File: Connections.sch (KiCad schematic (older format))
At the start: 12 parts, among them P4 CONN_02X07, P6 CONN_02X07, P7 CONN_02X07, P8 CONN_02X07, SW1 SW_PUSH, SW2 SW_PUSH

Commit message: Layouting
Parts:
- added P2: CONN_02X03, w_pin_strip:pin_strip_3x2, symbol CONN_02X03
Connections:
- net C_IO2: now also P2.5 (P5); no longer P6.3 (P3)
- net C_IO3: now also P2.4 (P4); no longer P6.4 (P4)
- new net C_IO1: P2.3 (P3)
- new net C_IO4: P2.6 (P6)
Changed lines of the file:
@@
 	1    0    0    -1
 $EndComp
-Text Label 6450 3650 0    60   ~ 0
-C_IO3
-Text Label 5600 3650 0    60   ~ 0
-C_IO2
 $Comp
 L CONN_02X07 P6
@@
 	5300 3400 6900 3400
 Wire Bus Line
-	5500 3400 5500 3950
+	5500 3400 5500 4050
 Wire Wire Line
 	5600 3750 5950 3750
@@
 	5600 4050 5950 4050
 Wire Bus Line
-	5500 4050 5500 3900
+	5500 3950 5500 3900
 Wire Wire Line
 	6800 4150 6450 4150
@@
 Text Label 6450 3750 0    60   ~ 0
 GPIO310
-Entry Wire Line
-	6800 3650 6900 3550
-Entry Wire Line
-	5500 3550 5600 3650
-Wire Wire Line
-	6450 3650 6800 3650
-Wire Wire Line
-	5950 3650 5600 3650
 Wire Wire Line
 	5950 3550 5950 3250
@@
 Wire Wire Line
 	6650 3550 6650 3150
+$Comp
+L CONN_02X03 P2
+U 1 1 578EC111
+P 6200 4800
+F 0 "P2" H 6200 5000 50  0000 C CNN
+F 1 "CONN_02X03" H 6200 4600 50  0000 C CNN
+F 2 "w_pin_strip:pin_strip_3x2" H 6200 3600 50  0001 C CNN
+F 3 "" H 6200 3600 50  0000 C CNN
+	1    6200 4800
+	1    0    0    -1
+$EndComp
+Text HLabel 5500 4550 0    60   BiDi ~ 0
+C_IO[1..6]
+Wire Bus Line
+	5500 4550 6900 4550
+Wire Bus Line
+	6900 4550 6900 5000
+Wire Bus Line
+	5650 4550 5650 5000
+Entry Wire Line
+	5650 4800 5750 4900
+Entry Wire Line
+	5650 4700 5750 4800
+Entry Wire Line
+	6800 4800 6900 4700
+Entry Wire Line
+	6800 4900 6900 4800
+Wire Wire Line
+	6450 4800 6800 4800
+Wire Wire Line
+	6450 4900 6800 4900
+Wire Wire Line
+	5950 4900 5750 4900
+Wire Wire Line
+	5950 4800 5750 4800
+Text Label 5750 4800 0    60   ~ 0
+C_IO1
+Text Label 5750 4900 0    60   ~ 0
+C_IO2
+Text Label 6450 4800 0    60   ~ 0
+C_IO3
+Text Label 6450 4900 0    60   ~ 0
+C_IO4
 $EndSCHEMATC

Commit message: Layout
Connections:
- net GND: now also P2.2 (P2), R15.1, R17.1, R18.1; no longer D5.1 (K), D6.1 (K), D7.1 (K)
- net LED1: now also D6.2 (A); no longer R17.2
- net LED2: now also D5.2 (A); no longer R15.2
- net LED3: now also D7.2 (A); no longer R18.2
- net VCC: now also P2.1 (P1)
- new net: D5.1 (K), R17.2
- new net: D6.1 (K), R15.2
- new net: D7.1 (K), R18.2
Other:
- moved on the sheet: D5, D6, D7, R15, R17, R18
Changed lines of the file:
@@
 LIBS:switches
 LIBS:xo-14s
+LIBS:oscillator_xo
 LIBS:FPGABoard-cache
 EELAYER 25 0
@@
 L LED D5
 U 1 1 57491075
-P 4150 1900
-F 0 "D5" H 4150 2000 50  0000 C CNN
-F 1 "LED" H 4150 1800 50  0000 C CNN
-F 2 "LEDs:LED_0805" H 4150 1900 50  0001 C CNN
-F 3 "" H 4150 1900 50  0000 C CNN
-	1    4150 1900
+P 3800 1900
+F 0 "D5" H 3800 2000 50  0000 C CNN
+F 1 "LED" H 3800 1800 50  0000 C CNN
+F 2 "LEDs:LED_0805" H 3800 1900 50  0001 C CNN
+F 3 "" H 3800 1900 50  0000 C CNN
+	1    3800 1900
 	-1   0    0    1
 $EndComp
@@
 L R R15
 U 1 1 5749111D
-P 3750 1900
-F 0 "R15" V 3830 1900 50  0000 C CNN
-F 1 "180R" V 3750 1900 50  0000 C CNN
-F 2 "Resistors_SMD:R_0805_HandSoldering" V 3680 1900 50  0001 C CNN
-F 3 "" H 3750 1900 50  0000 C CNN
-	1    3750 1900
+P 4200 1600
+F 0 "R15" V 4280 1600 50  0000 C CNN
+F 1 "180R" V 4200 1600 50  0000 C CNN
+F 2 "Resistors_SMD:R_0805_HandSoldering" V 4130 1600 50  0001 C CNN
+F 3 "" H 4200 1600 50  0000 C CNN
+	1    4200 1600
 	0    1    1    0
 $EndComp
@@
 L LED D6
 U 1 1 5782E4FA
-P 4150 1600
-F 0 "D6" H 4150 1700 50  0000 C CNN
-F 1 "LED" H 4150 1500 50  0000 C CNN
-F 2 "LEDs:LED_0805" H 4150 1600 50  0001 C CNN
-F 3 "" H 4150 1600 50  0000 C CNN
-	1    4150 1600
+P 3800 1600
+F 0 "D6" H 3800 1700 50  0000 C CNN
+F 1 "LED" H 3800 1500 50  0000 C CNN
+F 2 "LEDs:LED_0805" H 3800 1600 50  0001 C CNN
+F 3 "" H 3800 1600 50  0000 C CNN
+	1    3800 1600
 	-1   0    0    1
 $EndComp
@@
 L R R17
 U 1 1 5782E548
-P 3750 1600
-F 0 "R17" V 3830 1600 50  0000 C CNN
-F 1 "180R" V 3750 1600 50  0000 C CNN
-F 2 "Resistors_SMD:R_0805_HandSoldering" V 3680 1600 50  0001 C CNN
-F 3 "" H 3750 1600 50  0000 C CNN
-	1    3750 1600
+P 4200 1900
+F 0 "R17" V 4280 1900 50  0000 C CNN
+F 1 "180R" V 4200 1900 50  0000 C CNN
+F 2 "Resistors_SMD:R_0805_HandSoldering" V 4130 1900 50  0001 C CNN
+F 3 "" H 4200 1900 50  0000 C CNN
+	1    4200 1900
 	0    1    1    0
 $EndComp
@@
 L LED D7
 U 1 1 5782F410
-P 4150 2200
-F 0 "D7" H 4150 2300 50  0000 C CNN
-F 1 "LED" H 4150 2100 50  0000 C CNN
-F 2 "LEDs:LED_0805" H 4150 2200 50  0001 C CNN
-F 3 "" H 4150 2200 50  0000 C CNN
-	1    4150 2200
+P 3800 2200
+F 0 "D7" H 3800 2300 50  0000 C CNN
+F 1 "LED" H 3800 2100 50  0000 C CNN
+F 2 "LEDs:LED_0805" H 3800 2200 50  0001 C CNN
+F 3 "" H 3800 2200 50  0000 C CNN
+	1    3800 2200
 	-1   0    0    1
 $EndComp
@@
 L R R18
 U 1 1 5782F4A7
-P 3750 2200
-F 0 "R18" V 3830 2200 50  0000 C CNN
-F 1 "180R" V 3750 2200 50  0000 C CNN
-F 2 "Resistors_SMD:R_0805_HandSoldering" V 3680 2200 50  0001 C CNN
-F 3 "" H 3750 2200 50  0000 C CNN
-	1    3750 2200
+P 4200 2200
+F 0 "R18" V 4280 2200 50  0000 C CNN
+F 1 "180R" V 4200 2200 50  0000 C CNN
+F 2 "Resistors_SMD:R_0805_HandSoldering" V 4130 2200 50  0001 C CNN
+F 3 "" H 4200 2200 50  0000 C CNN
+	1    4200 2200
 	0    1    1    0
 $EndComp
@@
 	4350 2200 4450 2200
 Connection ~ 4450 2200
-Wire Wire Line
-	3900 2200 3950 2200
-Wire Wire Line
-	3900 1900 3950 1900
-Wire Wire Line
-	3900 1600 3950 1600
 Wire Bus Line
 	3000 1600 3300 1600
@@
 $EndComp
 Text HLabel 5500 4550 0    60   BiDi ~ 0
-C_IO[1..6]
+C_IO[1..4]
 Wire Bus Line
 	5500 4550 6900 4550
 Wire Bus Line
-	6900 4550 6900 5000
-Wire Bus Line
-	5650 4550 5650 5000
+	6900 4550 6900 4800
+Wire Bus Line
+	5650 4550 5650 4800
 Entry Wire Line
 	5650 4800 5750 4900
@@
 Text Label 6450 4900 0    60   ~ 0
 C_IO4
+Wire Wire Line
+	4000 1600 4050 1600
+Wire Wire Line
+	4000 1900 4050 1900
+Wire Wire Line
+	4000 2200 4050 2200
+$Comp
+L VCC #PWR028
+U 1 1 5793AA8D
+P 5900 4450
+F 0 "#PWR028" H 5900 4300 50  0001 C CNN
+F 1 "VCC" H 5900 4600 50  0000 C CNN
+F 2 "" H 5900 4450 50  0000 C CNN
+F 3 "" H 5900 4450 50  0000 C CNN
+	1    5900 4450
+	1    0    0    -1
+$EndComp
+$Comp
+L GND #PWR029
+U 1 1 5793AC86
+P 6600 4300
+F 0 "#PWR029" H 6600 4050 50  0001 C CNN
+F 1 "GND" H 6600 4150 50  0000 C CNN
+F 2 "" H 6600 4300 50  0000 C CNN
+F 3 "" H 6600 4300 50  0000 C CNN
+	1    6600 4300
+	1    0    0    -1
+$EndComp
+Wire Wire Line
+	5900 4450 5900 4700
+Wire Wire Line
+	5900 4700 5950 4700
+Wire Wire Line
+	6450 4700 6600 4700
+Wire Wire Line
+	6600 4700 6600 4300
 $EndSCHEMATC

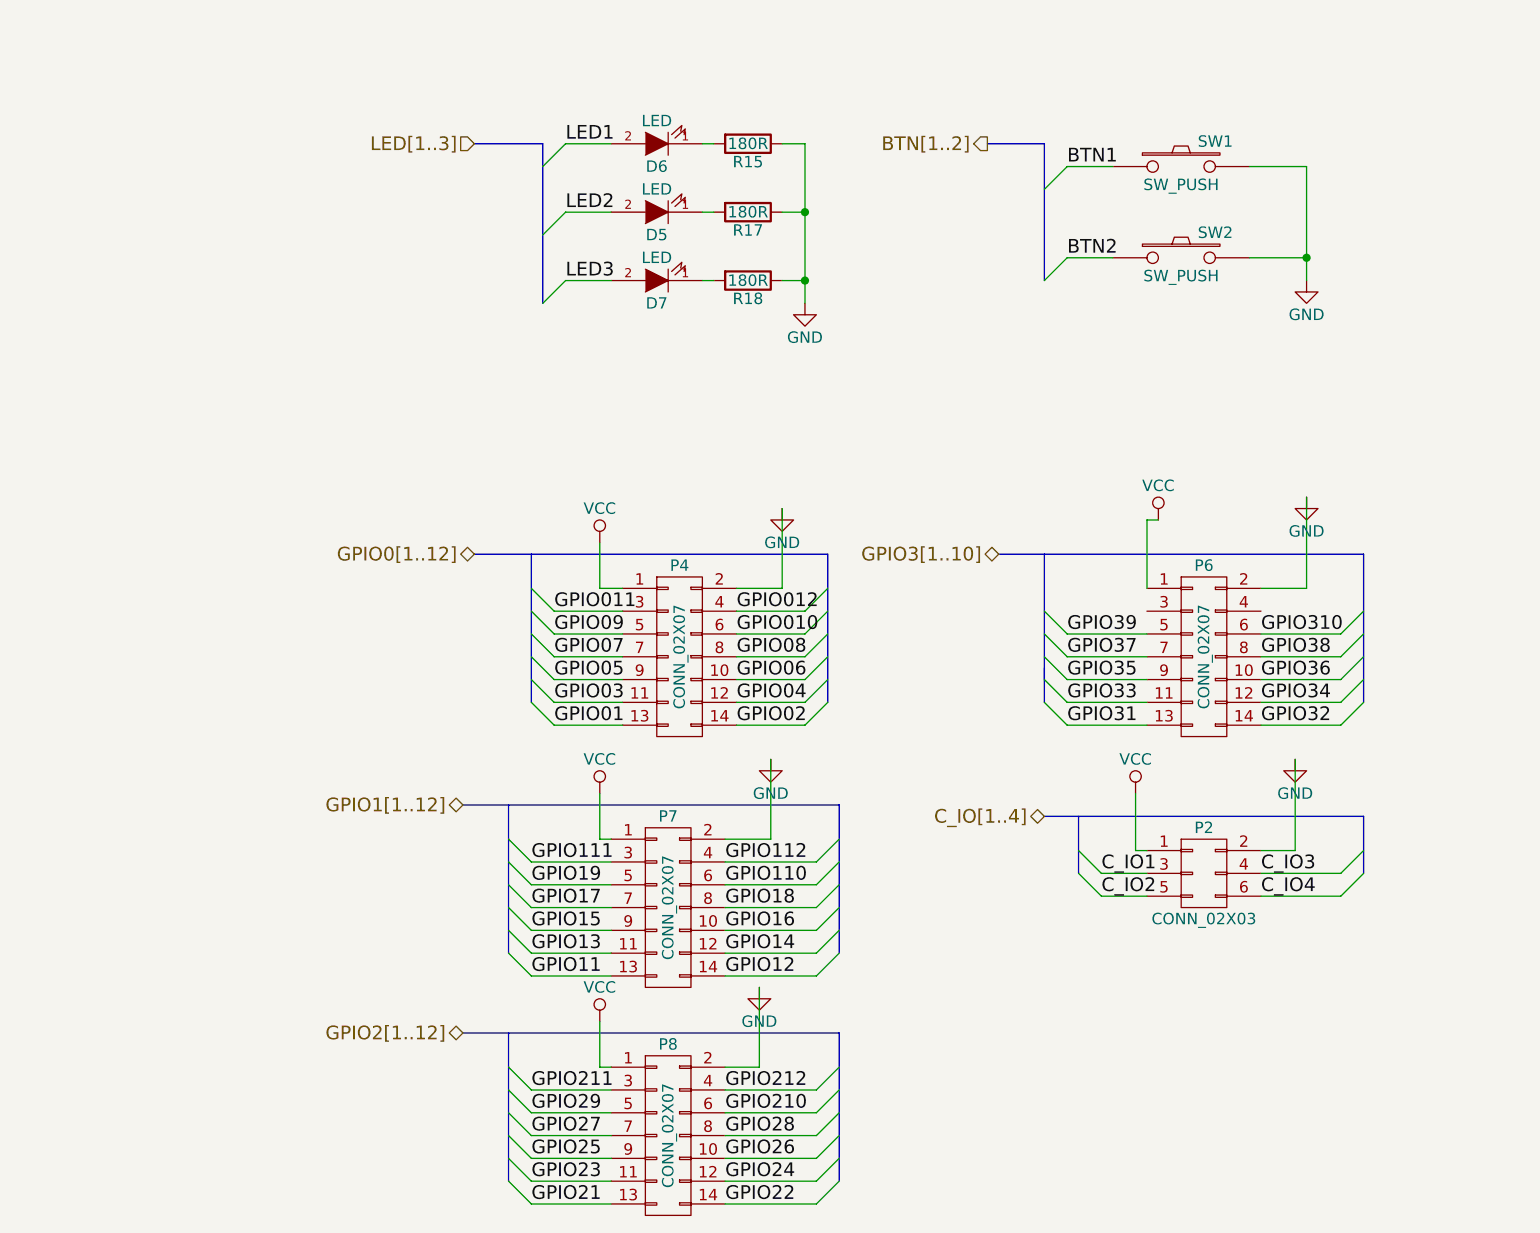
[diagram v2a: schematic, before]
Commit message: Additional Caps at VCC, Layout
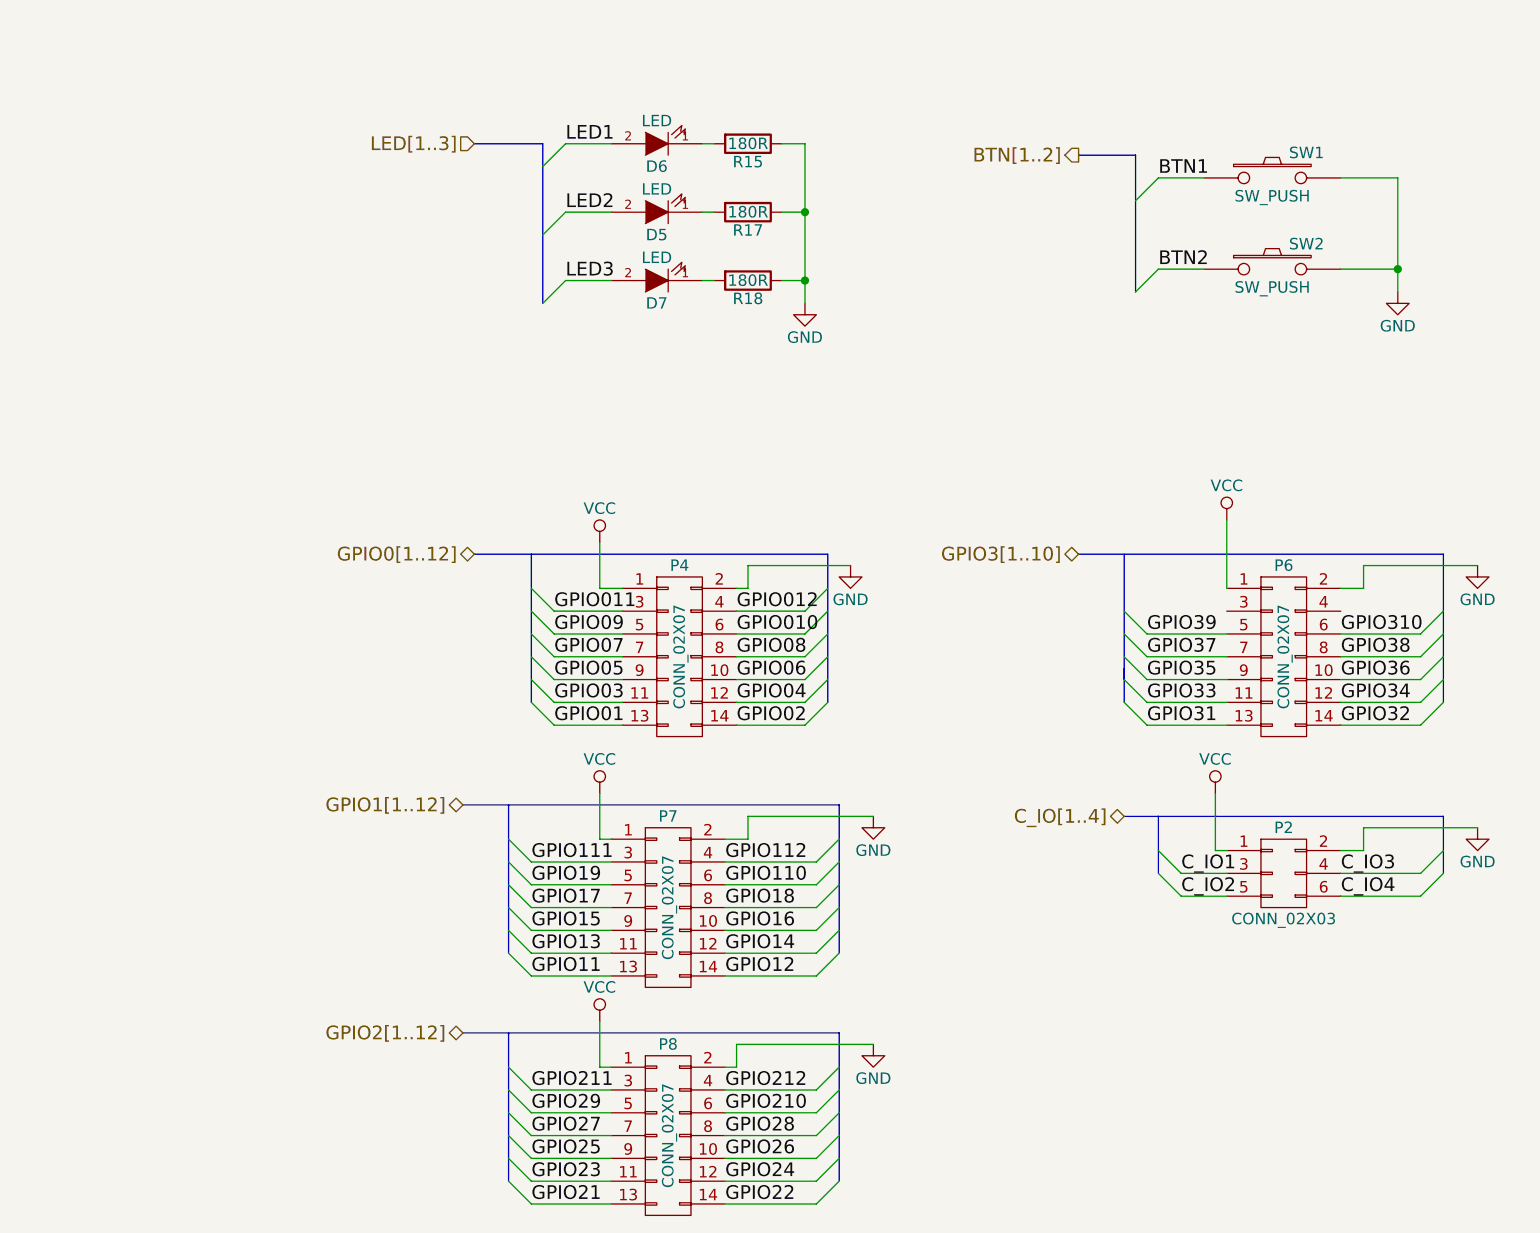
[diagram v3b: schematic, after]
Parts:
- P2: footprint w_pin_strip:pin_strip_3x2 -> Pin_Headers:Pin_Header_Straight_2x03
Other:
- moved on the sheet: P2, P6, SW1, SW2

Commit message: Work in Progress
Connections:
- no-connect marks 0 -> 2
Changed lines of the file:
@@
 Wire Wire Line
 	4200 4550 4750 4550
+NoConn ~ 6800 3650
+NoConn ~ 6300 3650
 $EndSCHEMATC

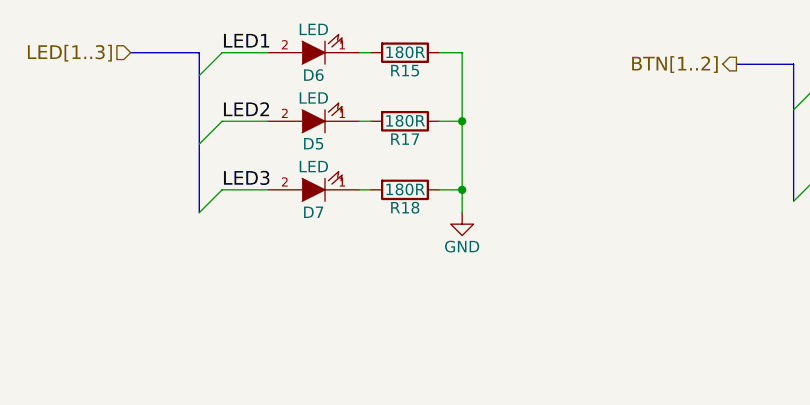
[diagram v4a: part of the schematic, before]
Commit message: All Resistors 0805, New Buttons
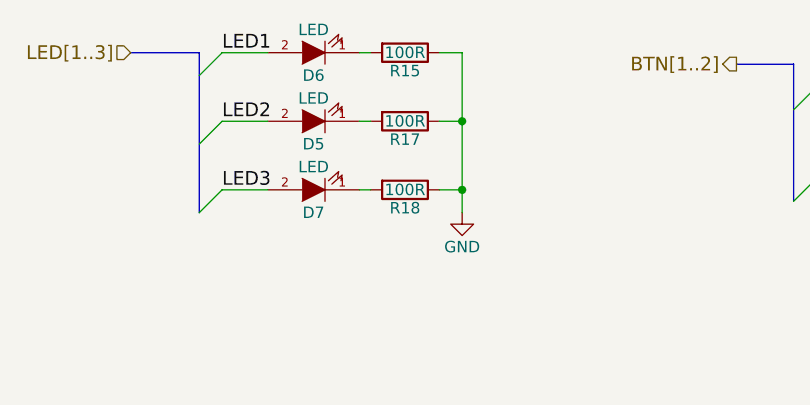
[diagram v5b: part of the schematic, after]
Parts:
- R15, R17, R18: value 180R -> 100R
- SW1, SW2: footprint Buttons_Switches_SMD:SW_SPST_B3S-1000 -> SMD_Switch_LSX1301:SW_LSx_1301
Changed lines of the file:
@@
 P 4200 1600
 F 0 "R15" V 4280 1600 50  0000 C CNN
-F 1 "180R" V 4200 1600 50  0000 C CNN
+F 1 "100R" V 4200 1600 50  0000 C CNN
 F 2 "Resistors_SMD:R_0805_HandSoldering" V 4130 1600 50  0001 C CNN
 F 3 "" H 4200 1600 50  0000 C CNN
@@
 F 0 "SW1" H 6650 1860 50  0000 C CNN
 F 1 "SW_PUSH" H 6500 1670 50  0000 C CNN
-F 2 "Buttons_Switches_SMD:SW_SPST_B3S-1000" H 6500 1750 50  0001 C CNN
+F 2 "SMD_Switch_LSX1301:SW_LSx_1301" H 6500 1750 50  0001 C CNN
 F 3 "" H 6500 1750 50  0000 C CNN
 	1    6500 1750
@@
 F 0 "SW2" H 6650 2260 50  0000 C CNN
 F 1 "SW_PUSH" H 6500 2070 50  0000 C CNN
-F 2 "Buttons_Switches_SMD:SW_SPST_B3S-1000" H 6500 2150 50  0001 C CNN
+F 2 "SMD_Switch_LSX1301:SW_LSx_1301" H 6500 2150 50  0001 C CNN
 F 3 "" H 6500 2150 50  0000 C CNN
 	1    6500 2150
@@
 P 4200 1900
 F 0 "R17" V 4280 1900 50  0000 C CNN
-F 1 "180R" V 4200 1900 50  0000 C CNN
+F 1 "100R" V 4200 1900 50  0000 C CNN
 F 2 "Resistors_SMD:R_0805_HandSoldering" V 4130 1900 50  0001 C CNN
 F 3 "" H 4200 1900 50  0000 C CNN
@@
 P 4200 2200
 F 0 "R18" V 4280 2200 50  0000 C CNN
-F 1 "180R" V 4200 2200 50  0000 C CNN
+F 1 "100R" V 4200 2200 50  0000 C CNN
 F 2 "Resistors_SMD:R_0805_HandSoldering" V 4130 2200 50  0001 C CNN
 F 3 "" H 4200 2200 50  0000 C CNN

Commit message: Ready for Production
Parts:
- removed P2: CONN_02X03, Pin_Headers:Pin_Header_Straight_2x03, symbol CONN_02X03
- added D10, D11, D12, D13: ZD3.6, Diodes_SMD:D_SOT-23_ANK, symbol D_Zener
- added R19, R20: 1k, Resistors_SMD:R_0805_HandSoldering, symbol R
- D5, D6, D7: value LED -> Green; symbol LED -> LED-RESCUE-FPGABoard
- R15, R17, R18: value 100R -> 36R
- SW1, SW2: symbol SW_PUSH -> SW_PUSH-RESCUE-FPGABoard
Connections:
- net BTN1: now also R19.1
- net BTN2: now also R20.1
- net GND: now also D10.2 (A), D11.2 (A), D12.2 (A), D13.2 (A)
- net VCC: now also D10.1 (K), D11.1 (K), D12.1 (K), D13.1 (K), R19.2, R20.2
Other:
- note added: "Nah an Steckerleisten"
- moved on the sheet: SW1, SW2
